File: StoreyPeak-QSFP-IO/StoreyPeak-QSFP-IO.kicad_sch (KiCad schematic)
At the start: 21 parts, among them J1 USB_B_Micro, J2 HDMI_A_1.4, U1 QSFP_PCB-QSFP, U2 FT232RL

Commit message: Changes
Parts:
- removed D1: RX, LED_SMD:LED_0805_2012Metric_Pad1.15x1.40mm_HandSolder, symbol Device:LED
- removed D2: TX, LED_SMD:LED_0805_2012Metric_Pad1.15x1.40mm_HandSolder, symbol Device:LED
- removed J2: HDMI_A_1.4, CarlosEDP_Lib:CONN-10029449-111RLF, symbol Connector:HDMI_A_1.4
- removed R7, R8: 47, Resistor_SMD:R_0603_1608Metric_Pad0.98x0.95mm_HandSolder, symbol Device:R
- added HDMI1: HD-A-05H9191N, easyeda2kicad:HDMI-SMD_HD-A-05H9192N, symbol easyeda2kicad:HD-A-05H9191N
- C10, C3, C4, C5, C6, C7, C8, C9: LCSC (none) -> C6119866
- C2: value (none) -> 10u; footprint (none) -> Capacitor_SMD:C_0603_1608Metric_Pad1.08x0.95mm_HandSolder
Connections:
- net +5V: now also HDMI1.18 (+5V)
- net GND: now also HDMI1.11 (CK_SHIELD), HDMI1.17 (GND), HDMI1.2 (D2_SHIELD), HDMI1.20 (SHD), HDMI1.21 (SHD), HDMI1.22 (SHD), HDMI1.23 (SHD), HDMI1.5 (D1_SHIELD), HDMI1.8 (D0_SHIELD)
- net HDMI_CLK+: now also HDMI1.10 (CK+)
- net HDMI_CLK-: now also HDMI1.12 (CK-)
- net HDMI_D0+: now also HDMI1.7 (D0+)
- net HDMI_D0-: now also HDMI1.9 (D0-)
- net HDMI_D1+: now also HDMI1.4 (D1+)
- net HDMI_D1-: now also HDMI1.6 (D1-)
- net HDMI_D2+: now also HDMI1.1 (D2+)
- net HDMI_D2-: now also HDMI1.3 (D2-)
- net USB_D+: now reaches J1.3 (D+), U2.15 (USBD+)
- net USB_D-: now reaches J1.2 (D-), U2.16 (USBD-)
- no-connect marks 35 -> 37
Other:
- moved on the sheet: C10, C3, C4, C5, C6, C7, C9

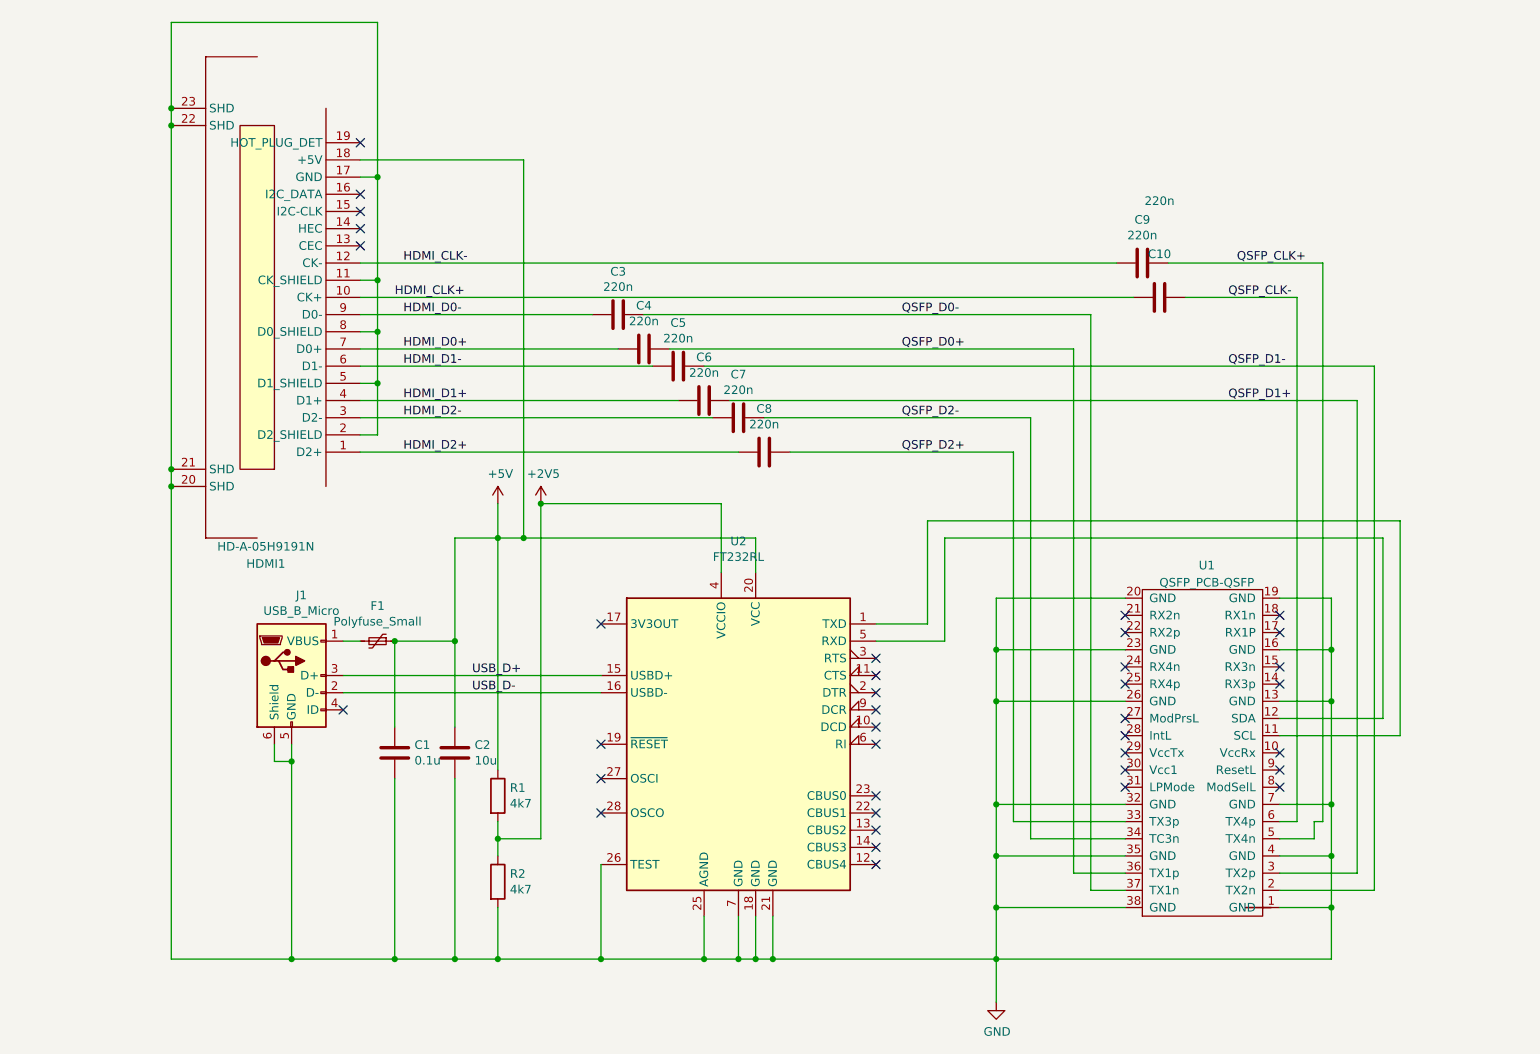
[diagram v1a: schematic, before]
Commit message: Use CH340G UART and USB-C port
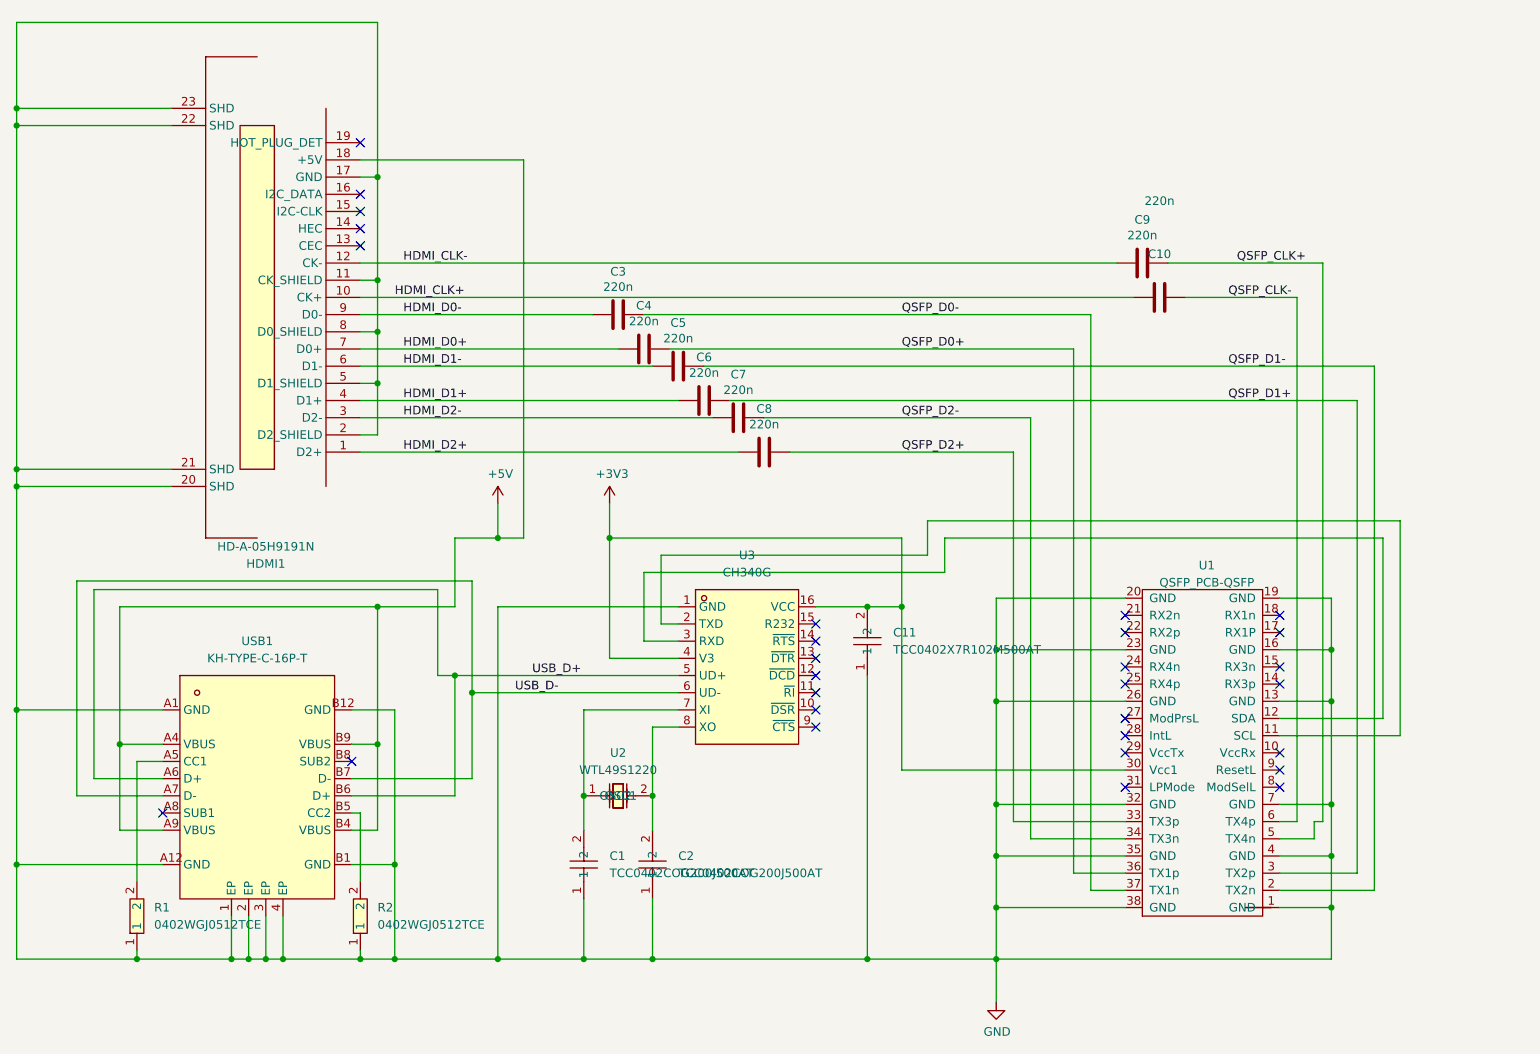
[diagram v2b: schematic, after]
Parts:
- removed C1: 0.1u, Capacitor_SMD:C_0603_1608Metric_Pad1.08x0.95mm_HandSolder, symbol Device:C
- removed C2: 10u, Capacitor_SMD:C_0603_1608Metric_Pad1.08x0.95mm_HandSolder, symbol Device:C
- removed F1: Polyfuse_Small, Fuse:Fuse_0603_1608Metric_Pad1.05x0.95mm_HandSolder, symbol Device:Polyfuse_Small
- removed J1: USB_B_Micro, CarlosEDP_Lib:USB_Micro-B_Molex-105017-0001, symbol Connector:USB_B_Micro
- removed R1, R2: 4k7, Resistor_SMD:R_0603_1608Metric_Pad0.98x0.95mm_HandSolder, symbol Device:R
- removed U2: FT232RL, Package_SO:SSOP-28_5.3x10.2mm_P0.65mm, symbol Interface_USB:FT232RL
- added C1, C2: TCC0402COG200J500AT, easyeda2kicad:C0402, symbol easyeda2kicad:TCC0402COG200J500AT
- added C11: TCC0402X7R102M500AT, easyeda2kicad:C0402, symbol easyeda2kicad:TCC0402X7R102M500AT
- added R1, R2: 0402WGJ0512TCE, easyeda2kicad:R0402, symbol easyeda2kicad:0402WGJ0512TCE
- added U2: WTL49S1220, easyeda2kicad:CRYSTAL-TH_L11.1-W4.7, symbol easyeda2kicad:WTL49S1220
- added U3: CH340G, easyeda2kicad:SOIC-16_L9.9-W3.9-P1.27-LS6.0-BL, symbol easyeda2kicad:CH340G
- added USB1: KH-TYPE-C-16P-T, easyeda2kicad:USB-C-SMD_KH-TYPE-C-16P, symbol easyeda2kicad:KH-TYPE-C-16P-T
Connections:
- net +5V: now also USB1.A4 (VBUS), USB1.A9 (VBUS), USB1.B4 (VBUS), USB1.B9 (VBUS)
- net GND: now also C1.1, C11.1, C2.1, R1.1, R2.1, U3.1 (GND), USB1.1 (EP), USB1.2 (EP), USB1.3 (EP), USB1.4 (EP), USB1.A1 (GND), USB1.A12 (GND), USB1.B1 (GND), USB1.B12 (GND)
- net USB_D+: now also U3.5 (UD+), USB1.A6 (D+), USB1.B6 (D+)
- net USB_D-: now also U3.6 (UD-), USB1.A7 (D-), USB1.B7 (D-)
- net at U1.11 (SCL): now also U3.2 (TXD)
- net at U1.12 (SDA): now also U3.3 (RXD)
- net +3V3: now reaches U1.30 (Vcc1)
- net +3V3: now also C11.2, U3.16 (VCC), U3.4 (V3)
- new net: R1.2, USB1.A5 (CC1)
- new net: C1.2, U2.1 (OSC1), U3.7 (XI)
- new net: R2.2, USB1.B5 (CC2)
- new net: C2.2, U2.2 (OSC2), U3.8 (XO)
- no-connect marks 37 -> 29

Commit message: Use passives from JLCPCB basic library
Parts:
- removed C1, C2: TCC0402COG200J500AT, easyeda2kicad:C0402, symbol easyeda2kicad:TCC0402COG200J500AT
- removed C11: TCC0402X7R102M500AT, easyeda2kicad:C0402, symbol easyeda2kicad:TCC0402X7R102M500AT
- removed R1, R2: 0402WGJ0512TCE, easyeda2kicad:R0402, symbol easyeda2kicad:0402WGJ0512TCE
- added C1, C2: 0402CG200J500NT, easyeda2kicad:C0402, symbol easyeda2kicad:0402CG200J500NT
- added C11: 0402B102K500NT, easyeda2kicad:C0402, symbol easyeda2kicad:0402B102K500NT
- added R1, R2: 0402WGF5101TCE, easyeda2kicad:R0402, symbol easyeda2kicad:0402WGF5101TCE
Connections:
- net +3V3: now also C11.2
- net GND: now also C1.1, C11.1, C2.1, R1.1, R2.1
- net at USB1.A5 (CC1): now also R1.2
- net at U2.1 (OSC1), U3.7 (XI): now also C1.2
- net at USB1.B5 (CC2): now also R2.2
- net at U2.2 (OSC2), U3.8 (XO): now also C2.2

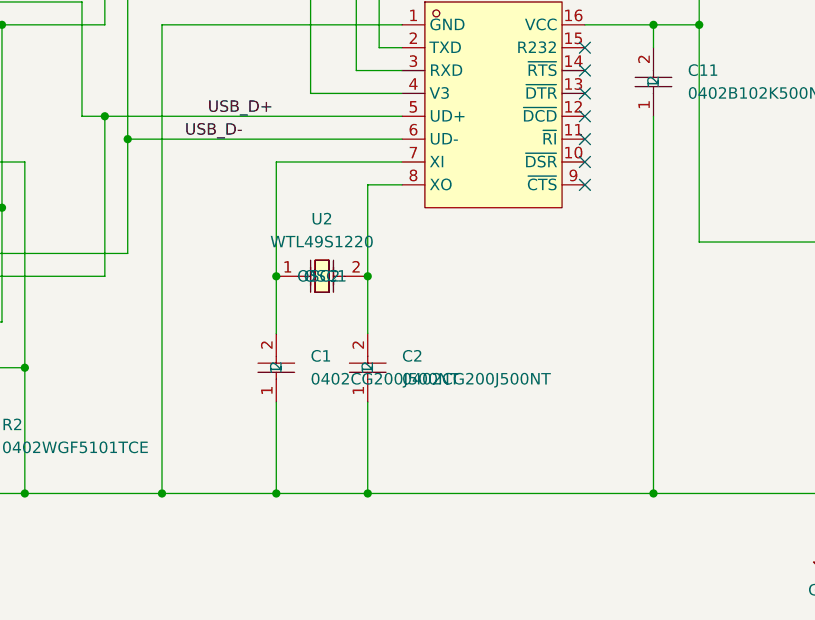
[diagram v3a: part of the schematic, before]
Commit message: Use SMD crystal instead of THT
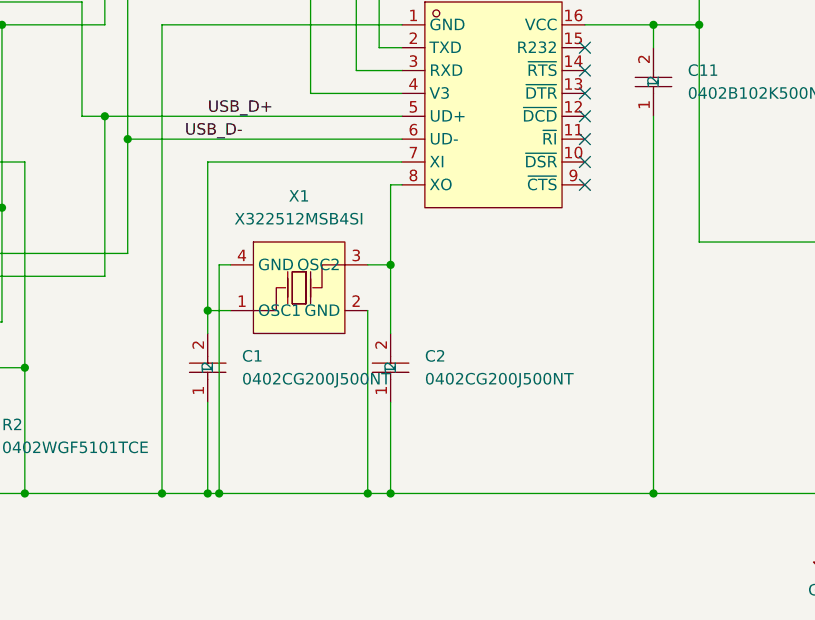
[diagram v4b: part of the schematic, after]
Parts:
- removed U2: WTL49S1220, easyeda2kicad:CRYSTAL-TH_L11.1-W4.7, symbol easyeda2kicad:WTL49S1220
- added X1: X322512MSB4SI, easyeda2kicad:CRYSTAL-SMD_4P-L3.2-W2.5-BL, symbol easyeda2kicad:X322512MSB4SI
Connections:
- net GND: now also X1.2 (GND), X1.4 (GND)
- net at C2.2, U3.8 (XO): now also X1.3 (OSC2)
- net at C1.2, U3.7 (XI): now also X1.1 (OSC1)
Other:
- moved on the sheet: C1, C2

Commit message: Replace more passives with JLCPCB basic parts
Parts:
- C10, C3, C4, C5, C6, C7, C8, C9: LCSC C6119866 -> C1604
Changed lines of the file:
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@@
 			)
 		)
-		(property "LCSC" "C6119866"
+		(property "LCSC" "C1604"
 			(at 105.41 60.96 90)
 			(effects
@@
 			)
 		)
-		(property "LCSC" "C6119866"
+		(property "LCSC" "C1604"
 			(at 109.22 66.04 90)
 			(effects
@@
 			)
 		)
-		(property "LCSC" "C6119866"
+		(property "LCSC" "C1604"
 			(at 114.3 68.58 90)
 			(effects
@@
 			)
 		)
-		(property "LCSC" "C6119866"
+		(property "LCSC" "C1604"
 			(at 118.11 73.66 90)
 			(effects
@@
 			)
 		)
-		(property "LCSC" "C6119866"
+		(property "LCSC" "C1604"
 			(at 123.19 76.2 90)
 			(effects
@@
 			)
 		)
-		(property "LCSC" "C6119866"
+		(property "LCSC" "C1604"
 			(at 127 81.28 90)
 			(effects
@@
 			)
 		)
-		(property "LCSC" "C6119866"
+		(property "LCSC" "C1604"
 			(at 182.88 53.34 90)
 			(effects
@@
 			)
 		)
-		(property "LCSC" "C6119866"
+		(property "LCSC" "C1604"
 			(at 185.42 58.42 90)
 			(effects

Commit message: Add test points, add screw holes to schematic
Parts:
- added H1, H2, H3, H4: MountingHole, MountingHole:MountingHole_2.2mm_M2, symbol Mechanical:MountingHole
- added TP1: 5V, TestPoint:TestPoint_Pad_1.5x1.5mm, symbol Connector:TestPoint
- added TP2: GND, TestPoint:TestPoint_Pad_1.5x1.5mm, symbol Connector:TestPoint
- added TP3: FPGA_RX, TestPoint:TestPoint_Pad_1.5x1.5mm, symbol Connector:TestPoint
- added TP4: FPGA_TX, TestPoint:TestPoint_Pad_1.5x1.5mm, symbol Connector:TestPoint
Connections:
- net +5V: now also TP1.1
- net GND: now also TP2.1
- net at U1.11 (SCL), U3.2 (TXD): now also TP3.1
- net at U1.12 (SDA), U3.3 (RXD): now also TP4.1

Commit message: Re-add vias (oops), add DP/DM pads, extend ground planes to cover entire board, stitch ground planes together
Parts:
- added TP5: DP, TestPoint:TestPoint_Pad_1.5x1.5mm, symbol Connector:TestPoint
- added TP6: DM, TestPoint:TestPoint_Pad_1.5x1.5mm, symbol Connector:TestPoint
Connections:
- net USB_D+: now also TP5.1
- net USB_D-: now also TP6.1
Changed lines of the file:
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@@
+	)
+	(junction
+		(at 86.36 116.84)
+		(diameter 0)
+		(color 0 0 0 0)
 	)
 	(junction
@@
 	)
 	(junction
+		(at 101.6 114.3)
+		(diameter 0)
+		(color 0 0 0 0)
+	)
+	(junction
 		(at 104.14 93.98)
 		(diameter 0)
@@
 	(wire
 		(pts
-			(xy 81.28 114.3) (xy 114.3 114.3)
+			(xy 81.28 114.3) (xy 101.6 114.3)
 		)
 		(stroke
@@
 	(wire
 		(pts
-			(xy 83.82 116.84) (xy 114.3 116.84)
+			(xy 83.82 116.84) (xy 86.36 116.84)
 		)
 		(stroke
@@
 	(wire
 		(pts
+			(xy 101.6 114.3) (xy 114.3 114.3)
+		)
+		(stroke
+			(width 0)
+			(type default)
+		)
+	)
+	(wire
+		(pts
 			(xy 203.2 140.97) (xy 210.82 140.97)
 		)
@@
 		(pts
 			(xy 180.34 118.11) (xy 161.29 118.11)
+		)
+		(stroke
+			(width 0)
+			(type default)
+		)
+	)
+	(wire
+		(pts
+			(xy 86.36 116.84) (xy 114.3 116.84)
 		)
 		(stroke
@@
 				(path "/09a4c8ee-e8d7-4980-8dc1-43a8ae75179d"
 					(reference "C10")
+					(unit 1)
+				)
+			)
+		)
+	)
+	(symbol
+		(lib_id "Connector:TestPoint")
+		(at 101.6 114.3 0)
+		(unit 1)
+		(exclude_from_sim no)
+		(in_bom yes)
+		(on_board yes)
+		(dnp no)
+		(property "Reference" "TP5"
+			(at 104.14 109.7279 0)
+			(effects
+				(font
+					(size 1.27 1.27)
+				)
+				(justify left)
+				(hide yes)
+			)
+		)
+		(property "Value" "DP"
+			(at 104.14 112.2679 0)
+			(effects
+				(font
+					(size 1.27 1.27)
+				)
+				(justify left)
+			)
+		)
+		(property "Footprint" "TestPoint:TestPoint_Pad_1.5x1.5mm"
+			(at 106.68 114.3 0)
+			(effects
+				(font
+					(size 1.27 1.27)
+				)
+				(hide yes)
+			)
+		)
+		(property "Datasheet" "~"
+			(at 106.68 114.3 0)
+			(effects
+				(font
+					(size 1.27 1.27)
+				)
+				(hide yes)
+			)
+		)
+		(property "Description" "test point"
+			(at 101.6 114.3 0)
+			(effects
+				(font
+					(size 1.27 1.27)
+				)
+				(hide yes)
+			)
+		)
+		(pin "1"
+		)
+		(instances
+			(project "StoreyPeak-QSFP-IO"
+				(path "/09a4c8ee-e8d7-4980-8dc1-43a8ae75179d"
+					(reference "TP5")
 					(unit 1)
 				)
@@
 					(unit 1)
 				)
+			)
+		)
+	)
+	(symbol
+		(lib_id "Connector:TestPoint")
+		(at 86.36 116.84 0)
+		(unit 1)
+		(exclude_from_sim no)
+		(in_bom yes)
+		(on_board yes)
+		(dnp no)
+		(property "Reference" "TP6"
+			(at 88.9 112.2679 0)
+			(effects
+				(font
+					(size 1.27 1.27)
+				)
+				(justify left)
+				(hide yes)
+			)
+		)
+		(property "Value" "DM"
+			(at 88.9 114.8079 0)
+			(effects
+				(font
+					(size 1.27 1.27)
+				)
+				(justify left)
+			)
+		)
+		(property "Footprint" "TestPoint:TestPoint_Pad_1.5x1.5mm"
+			(at 91.44 116.84 0)
+			(effects
+				(font
+					(size 1.27 1.27)
+				)
+				(hide yes)
+			)
+		)
+		(property "Datasheet" "~"
+			(at 91.44 116.84 0)
+			(effects
+				(font
+					(size 1.27 1.27)
+				)
+				(hide yes)
+			)
+		)
+		(property "Description" "test point"
+			(at 86.36 116.84 0)
+			(effects
+				(font
+					(size 1.27 1.27)
+				)
+				(hide yes)
+			)
+		)
+		(pin "1"
+		)
+		(instances
+			(project "StoreyPeak-QSFP-IO"
+				(path "/09a4c8ee-e8d7-4980-8dc1-43a8ae75179d"
+					(reference "TP6")
+					(unit 1)
+				)
